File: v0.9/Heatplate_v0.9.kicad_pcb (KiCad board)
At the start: 2 copper layers, 100 x 100 mm, 55 parts, among them J1 Barrel_Jack_Switch, Q1 WSP4409A, Q2 IRLR8726TRPBF, Q3 SS8050, SW1 SW_Push, SW2 SW_Push, U1 ATMEGA4809-AFR, U2 AMS1117-5.0

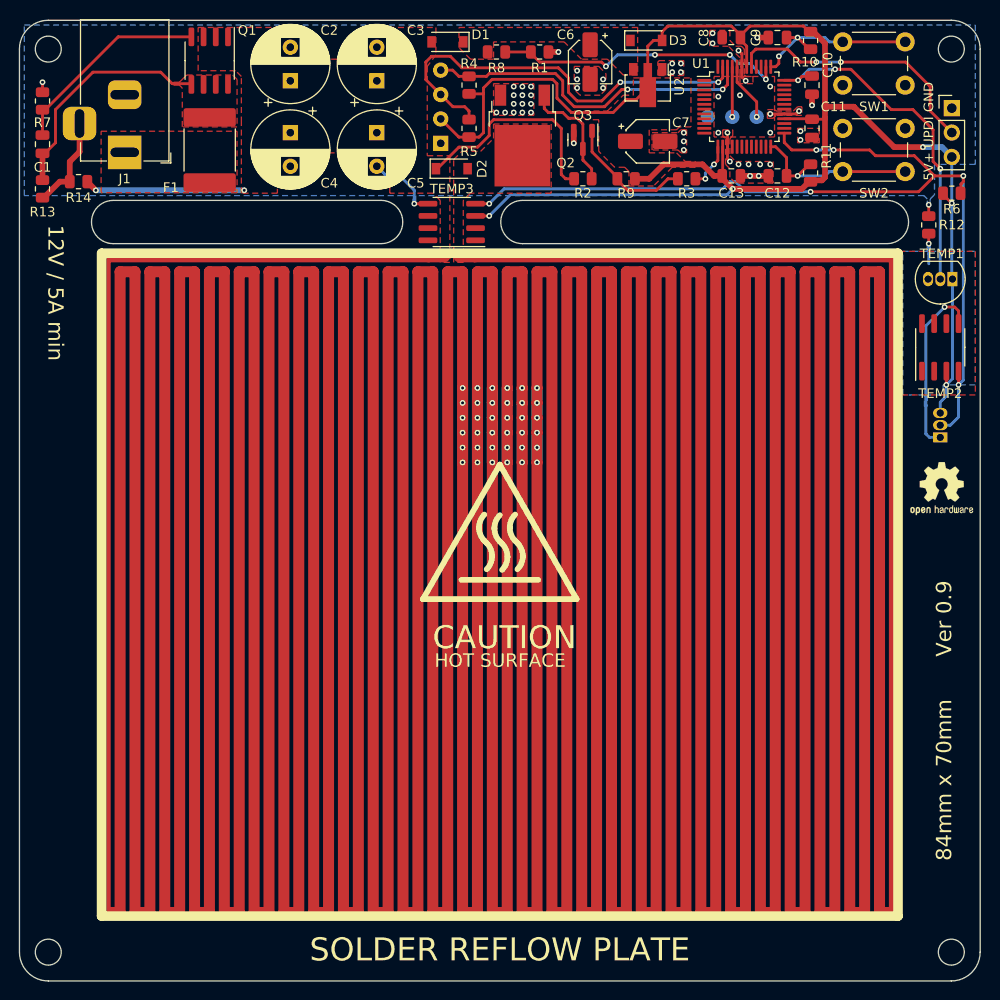
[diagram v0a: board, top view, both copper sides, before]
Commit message: Add files via upload
status LEDs added
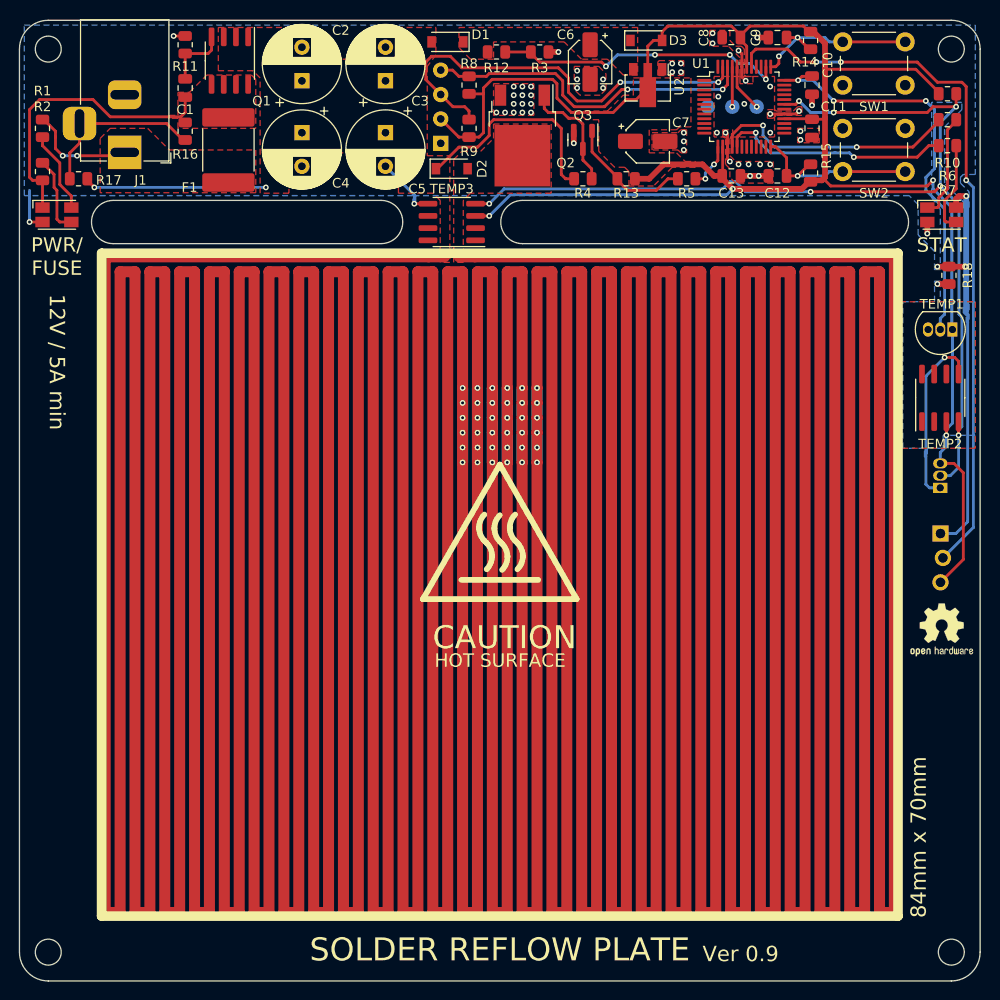
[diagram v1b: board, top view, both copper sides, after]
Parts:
- added LED1: RED/GREEN, LED_SMD:LED_Avago_PLCC4_3.2x2.8mm_CW, F.Cu at (63.9, 80.2)
- added LED2: RED/GREEN, LED_SMD:LED_Avago_PLCC4_3.2x2.8mm_CW, F.Cu at (156.0, 80.2)
- added R1: 1k, Resistor_SMD:R_0805_2012Metric, F.Cu at (62.4, 71.2)
- added R2: 1k, Resistor_SMD:R_0805_2012Metric, F.Cu at (62.4, 75.8)
- added R6: 1k, Resistor_SMD:R_0805_2012Metric, F.Cu at (156.6, 70.3)
- added R7: 1k, Resistor_SMD:R_0805_2012Metric, F.Cu at (156.6, 73.0)
- UPDI1: moved to B.Cu
- moved UPDI1 44.3 mm to (156.0, 113.4), turned to 180 degrees
- moved R16 16.0 mm to (77.2, 71.5)
- moved C1 16.0 mm to (77.2, 67.0)
- moved R11 16.0 mm to (77.2, 62.5)
- moved LOGO1 14.7 mm to (156.0, 123.5)
- moved R10 10.4 mm to (156.6, 67.7)
- moved R18 5.65 mm to (156.8, 86.5)
- moved TEMP1 5.25 mm to (157.1, 92.2)
- moved TEMP2 5.25 mm to (155.8, 99.3)
- moved TEMP4 5.25 mm to (155.8, 108.7)
- moved Q1 2.10 mm to (81.9, 64.2)
- moved F1 1.95 mm to (81.8, 73.5)
- moved C2 1.20 mm to (89.4, 66.3)
- moved C4 1.20 mm to (89.4, 71.7)
- moved TP1 1.05 mm to (136.7, 69.0)
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- renumbered R6 to R10, R7 to R11, R8 to R12, R9 to R13, R10 to R14, R11 to R15, R13 to R16, R14 to R17, R12 to R18, R1 to R3, R2 to R4, R3 to R5, R4 to R8, R5 to R9
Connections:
- U1 pad 16: unconnected-(U1-Pad16) -> /LED_R
- U1 pad 17: unconnected-(U1-Pad17) -> /LED_G
- U1 pad 25: /TDATA_D -> unconnected-(U1-Pad25)
- U1 pad 31: unconnected-(U1-Pad31) -> /TDATA_D
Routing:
- net /UPDI: track 27.5 -> 76.2 mm, vias 2 -> 3
- net GND: track 27.2 -> 73.3 mm, vias 54 -> 58
- net +5V: track 174.9 -> 201.7 mm, vias 5 -> 4
- net /LED_R: track 0.00 -> 26.0 mm, vias 0 -> 2
- net /LED_G: track 0.00 -> 24.1 mm, vias 0 -> 2
- net Net-(C1-Pad2): track 21.0 -> 6.91 mm
- net Net-(F1-Pad1): track 0.00 -> 11.5 mm, vias 0 -> 2
- net /TDATA_D: track 101.8 -> 113.1 mm, vias 6 -> 7
- net Net-(LED2-Pad1): track 0.00 -> 11.0 mm
- net Net-(LED2-Pad3): track 0.00 -> 9.56 mm
- net Net-(LED1-Pad1): track 0.00 -> 8.58 mm
- net Net-(LED1-Pad3): track 0.00 -> 8.11 mm
- net Net-(J1-Pad3): track 9.86 -> 17.9 mm
- net Net-(C1-Pad1): track 24.0 -> 30.5 mm
- net /TDATA_A: track 36.6 -> 42.8 mm
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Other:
- board text added: "PWR/ FUSE"
- board text added: "STAT"
- board text added: "UPDI"
- board text removed: "5V+ UPDI GND"

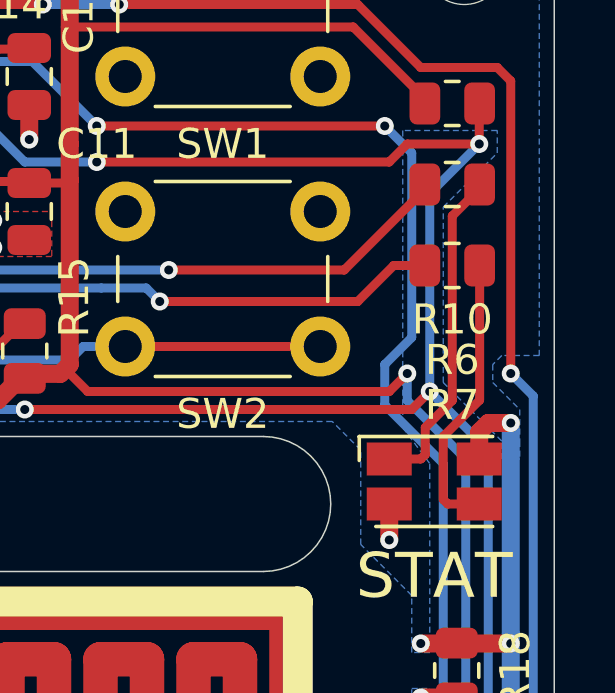
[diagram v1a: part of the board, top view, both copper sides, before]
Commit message: error in LED2 footprint fixed
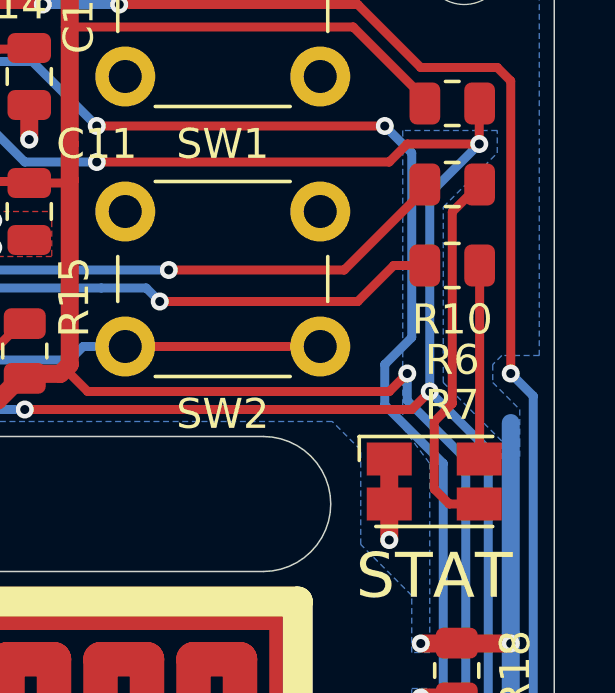
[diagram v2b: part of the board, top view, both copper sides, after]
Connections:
- LED2 pad 1: Net-(LED2-Pad1) -> Net-(R7-Pad2)
- LED2 pad 3: Net-(LED2-Pad3) -> Net-(R6-Pad2)
- R6 pad 1: /LED_R -> /LED_G
- R6 pad 2: Net-(LED2-Pad1) -> Net-(R6-Pad2)
- R7 pad 1: /LED_G -> /LED_R
- R7 pad 2: Net-(LED2-Pad3) -> Net-(R7-Pad2)
- U1 pad 16: /LED_R -> /LED_G
- U1 pad 17: /LED_G -> /LED_R
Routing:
- net Net-(R6-Pad2): track 0.00 -> 12.5 mm
- net Net-(LED2-Pad1): track 11.0 -> 0.00 mm
- net Net-(LED2-Pad3): track 9.56 -> 0.00 mm
- net Net-(R7-Pad2): track 0.00 -> 6.46 mm
- net /LED_R: track 26.0 -> 24.1 mm
- net /LED_G: track 24.1 -> 26.0 mm
- net GND: track 73.3 -> 72.7 mm, vias 58 -> 57
